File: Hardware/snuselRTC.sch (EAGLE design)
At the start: 22 parts, among them IC1 ATTINY24/44/84-SSU, T1 BF 820 SMD, U1 RV2123-C2

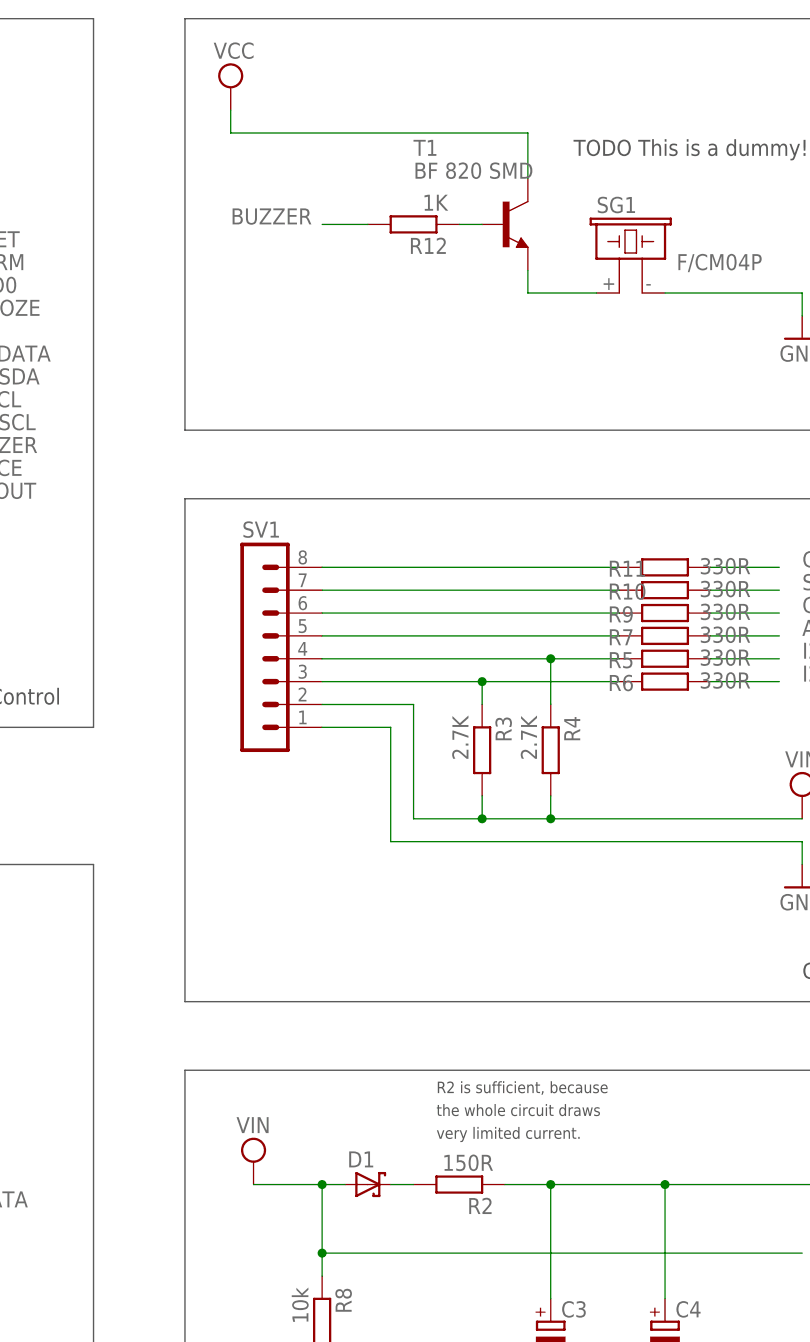
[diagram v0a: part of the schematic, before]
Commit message: Schematic: No transistor for Buzzer
The Buzzer draws 15 mA max, which can be provided by the µC.
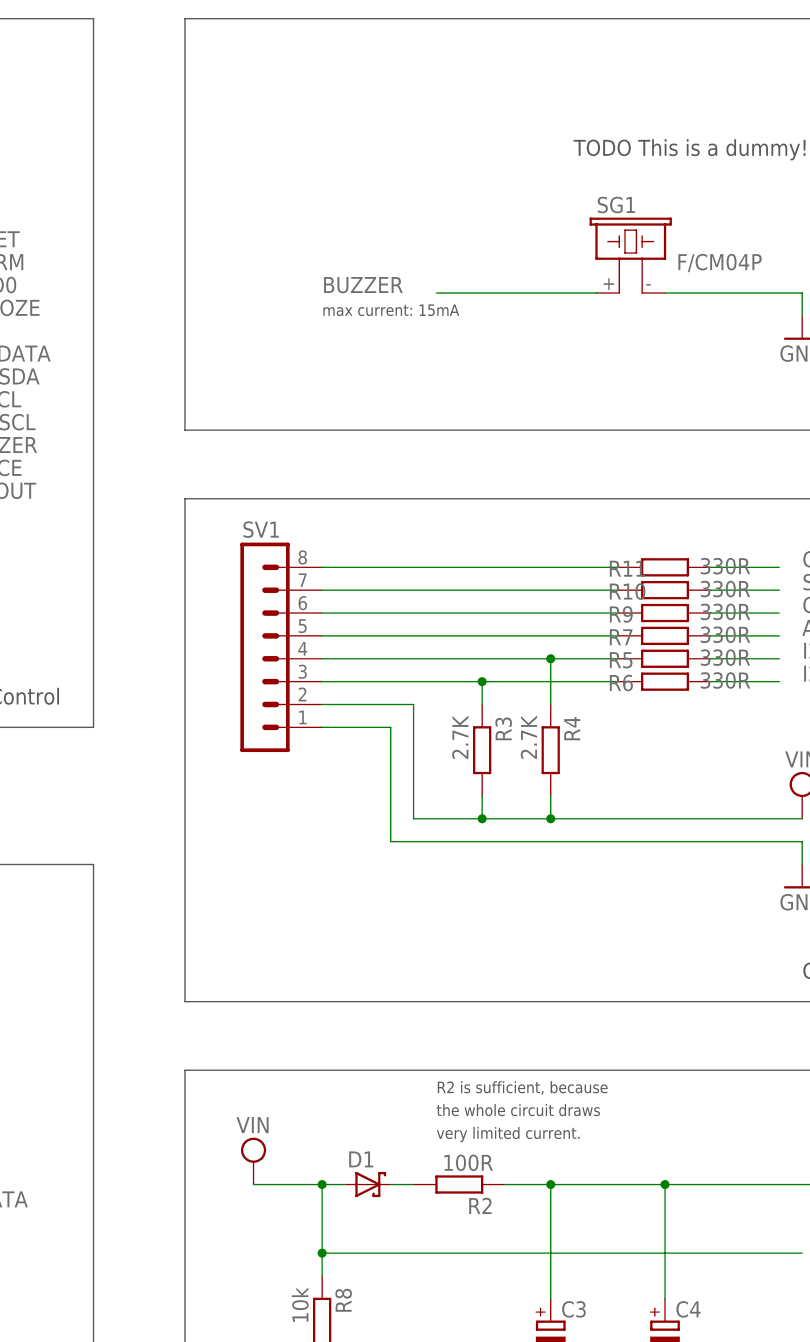
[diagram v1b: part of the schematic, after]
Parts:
- removed R12: 1K, resistor:R-EU_R0805
- removed T1: BF 820 SMD, transistor:BF820-NPN-SOT23-BEC
- R2: value 150R -> 100R
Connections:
- removed net N$10: R12.1, T1.B
- removed net N$8: SG1.1, T1.E
- net BUZZER: now also SG1.1; no longer R12.2
- net VCC: no longer T1.C
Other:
- note added: "max current: 15mA"
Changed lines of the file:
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@@
 <part name="GND3" library="supply1" deviceset="GND" device=""/>
 <part name="SUPPLY2" library="supply2" deviceset="VCC" device=""/>
-<part name="R2" library="resistor" deviceset="R-EU_" device="R0805" value="150R"/>
+<part name="R2" library="resistor" deviceset="R-EU_" device="R0805" value="100R"/>
 <part name="D1" library="diode" deviceset="SCHOTTKY-DIODE" device="SMD"/>
 <part name="VIN" library="supply2" deviceset="VCC" device="" value="VIN"/>
@@
 <part name="R10" library="resistor" deviceset="R-EU_" device="R0805" value="330R"/>
 <part name="R11" library="resistor" deviceset="R-EU_" device="R0805" value="330R"/>
-<part name="T1" library="transistor" deviceset="*-NPN-" device="SOT23-BEC" technology="BF820" value="BF 820 SMD"/>
 <part name="SG1" library="buzzer" deviceset="F/CM04P" device=""/>
-<part name="R12" library="resistor" deviceset="R-EU_" device="R0805" value="1K"/>
 <part name="GND6" library="supply1" deviceset="GND" device=""/>
-<part name="SUPPLY4" library="supply2" deviceset="VCC" device=""/>
 </parts>
 <sheets>
@@
 <wire x1="187.96" y1="170.18" x2="106.68" y2="170.18" width="0.1524" layer="97"/>
 <text x="177.8" y="127" size="1.778" layer="97">Buzzer</text>
+<text x="121.92" y="137.16" size="1.27" layer="97">max current: 15mA</text>
 </plain>
 <instances>
@@
 <attribute name="VALUE" x="163.83" y="108.458" size="1.778" layer="96"/>
 </instance>
-<instance part="T1" gate="G$1" x="142.24" y="147.32"/>
 <instance part="SG1" gate="G$1" x="154.94" y="142.24"/>
-<instance part="R12" gate="G$1" x="132.08" y="147.32" rot="R180"/>
 <instance part="GND6" gate="1" x="175.26" y="134.62"/>
-<instance part="SUPPLY4" gate="G$1" x="111.76" y="162.56"/>
 </instances>
 <busses>
@@
 <junction x="147.32" y="81.28"/>
 </segment>
-<segment>
-<pinref part="SUPPLY4" gate="G$1" pin="VCC"/>
-<wire x1="111.76" y1="160.02" x2="111.76" y2="157.48" width="0.1524" layer="91"/>
-<wire x1="111.76" y1="157.48" x2="144.78" y2="157.48" width="0.1524" layer="91"/>
-<pinref part="T1" gate="G$1" pin="C"/>
-<wire x1="144.78" y1="157.48" x2="144.78" y2="152.4" width="0.1524" layer="91"/>
-</segment>
 </net>
 <net name="BUZZER" class="0">
@@
 </segment>
 <segment>
-<wire x1="127" y1="147.32" x2="121.92" y2="147.32" width="0.1524" layer="91"/>
-<label x="111.76" y="147.32" size="1.778" layer="95"/>
-<pinref part="R12" gate="G$1" pin="2"/>
+<label x="121.92" y="139.7" size="1.778" layer="95"/>
+<pinref part="SG1" gate="G$1" pin="1"/>
+<wire x1="134.62" y1="139.7" x2="152.4" y2="139.7" width="0.1524" layer="91"/>
 </segment>
 </net>
@@
 </segment>
 </net>
-<net name="N$8" class="0">
-<segment>
-<pinref part="T1" gate="G$1" pin="E"/>
-<wire x1="144.78" y1="142.24" x2="144.78" y2="139.7" width="0.1524" layer="91"/>
-<pinref part="SG1" gate="G$1" pin="1"/>
-<wire x1="144.78" y1="139.7" x2="152.4" y2="139.7" width="0.1524" layer="91"/>
-</segment>
-</net>
-<net name="N$10" class="0">
-<segment>
-<pinref part="T1" gate="G$1" pin="B"/>
-<wire x1="137.16" y1="147.32" x2="139.7" y2="147.32" width="0.1524" layer="91"/>
-<pinref part="R12" gate="G$1" pin="1"/>
-</segment>
-</net>

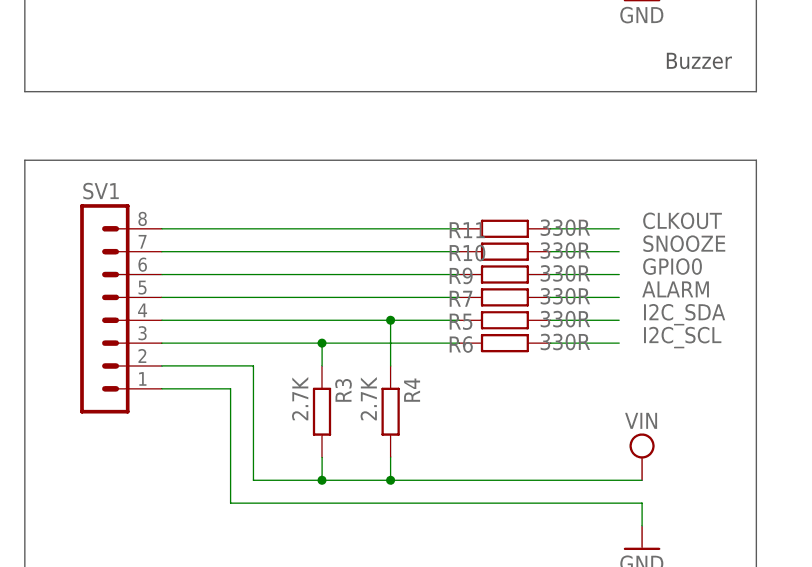
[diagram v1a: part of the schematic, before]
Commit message: Schematic: Remove the IO resistors
The SnuselRTC will be the last module that does not have power, so we do not need the IO protection.
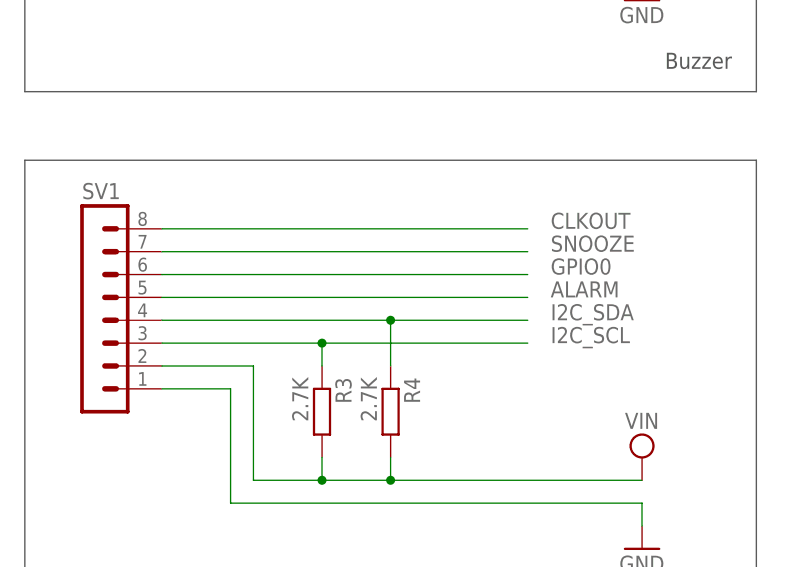
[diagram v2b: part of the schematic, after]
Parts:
- removed R10, R11, R5, R6, R7, R9: 330R, resistor:R-EU_R0805
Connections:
- removed net N$2: R3.1, R6.1, SV1.3
- removed net N$3: R4.1, R5.1, SV1.4
- removed net N$4: R7.1, SV1.5
- removed net N$5: R9.1, SV1.6
- removed net N$6: R10.1, SV1.7
- removed net N$7: R11.1, SV1.8
- net ALARM: now also SV1.5; no longer R7.2
- net CLKOUT: now also SV1.8; no longer R11.2
- net GPIO0: now also SV1.6; no longer R9.2
- net I2C_SCL: now also R3.1, SV1.3; no longer R6.2
- net I2C_SDA: now also R4.1, SV1.4; no longer R5.2
- net SNOOZE: now also SV1.7; no longer R10.2
